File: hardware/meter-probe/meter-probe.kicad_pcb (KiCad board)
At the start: 4 copper layers, 40 x 68 mm, 52 parts, among them J1 Cable, SW1 Sensor Button, U1 TSL2585, U2 USBLC6-2SC6, U3 MIC5365-1.8YC5, U4 FT260Q, U5 CAT24C08

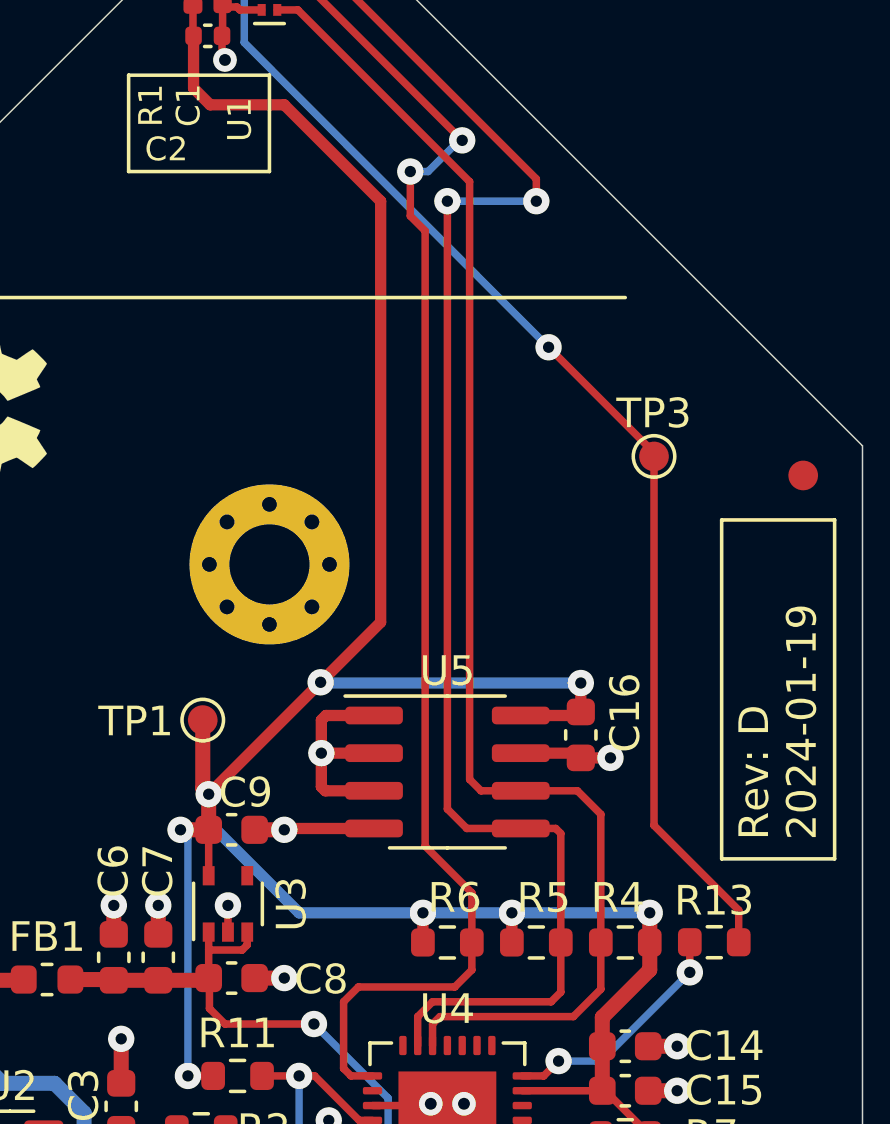
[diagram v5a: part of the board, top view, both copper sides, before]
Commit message: Change footprint of meter probe EEPROM
This change is for a smaller package, to better fit within enclosure
size constraints that limit height above the board on the front half.
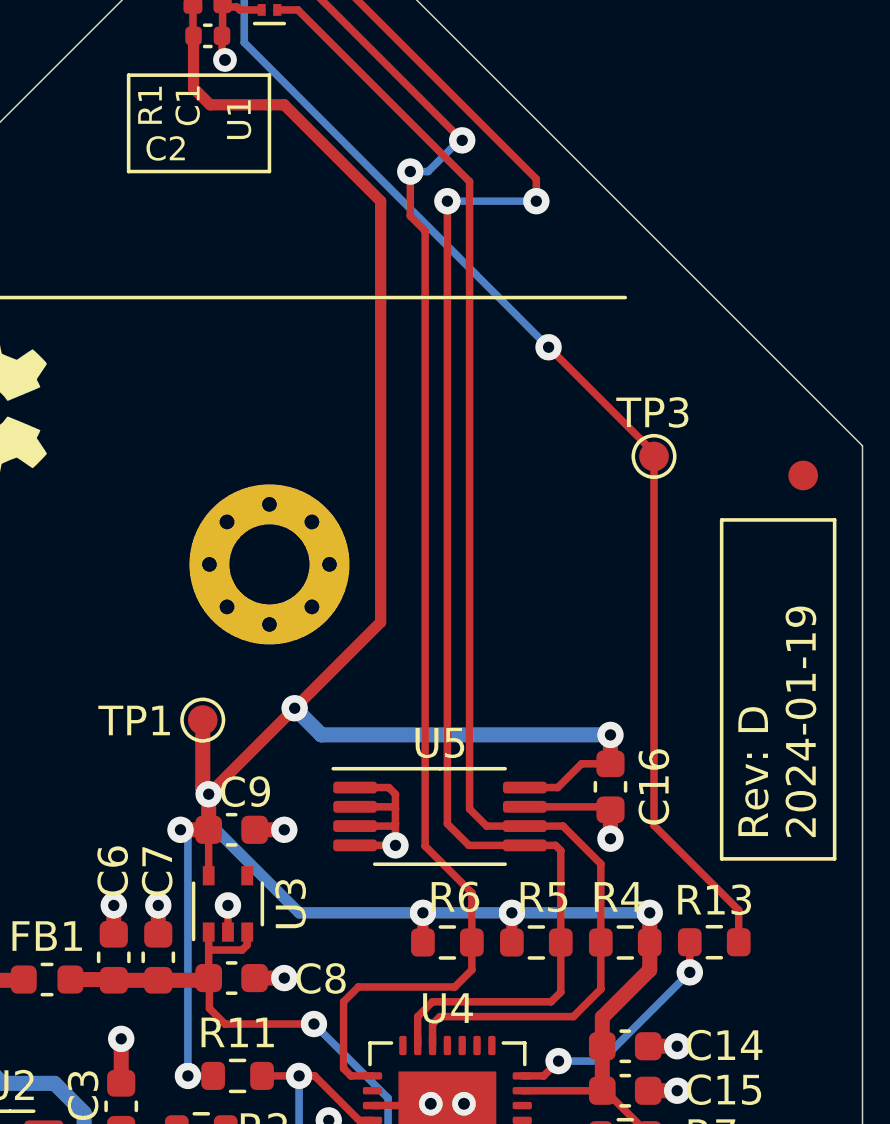
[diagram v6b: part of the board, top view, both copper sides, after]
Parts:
- U5: footprint Package_SO:SOIC-8_3.9x4.9mm_P1.27mm -> Package_SO:TSSOP-8_4.4x3mm_P0.65mm
- moved C16 2.02 mm to (131.5, 89.5)
- moved U5 1.52 mm to (125.8, 90.5)
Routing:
- net +1V8: track 93.8 -> 97.4 mm
- net GND: track 44.8 -> 42.3 mm

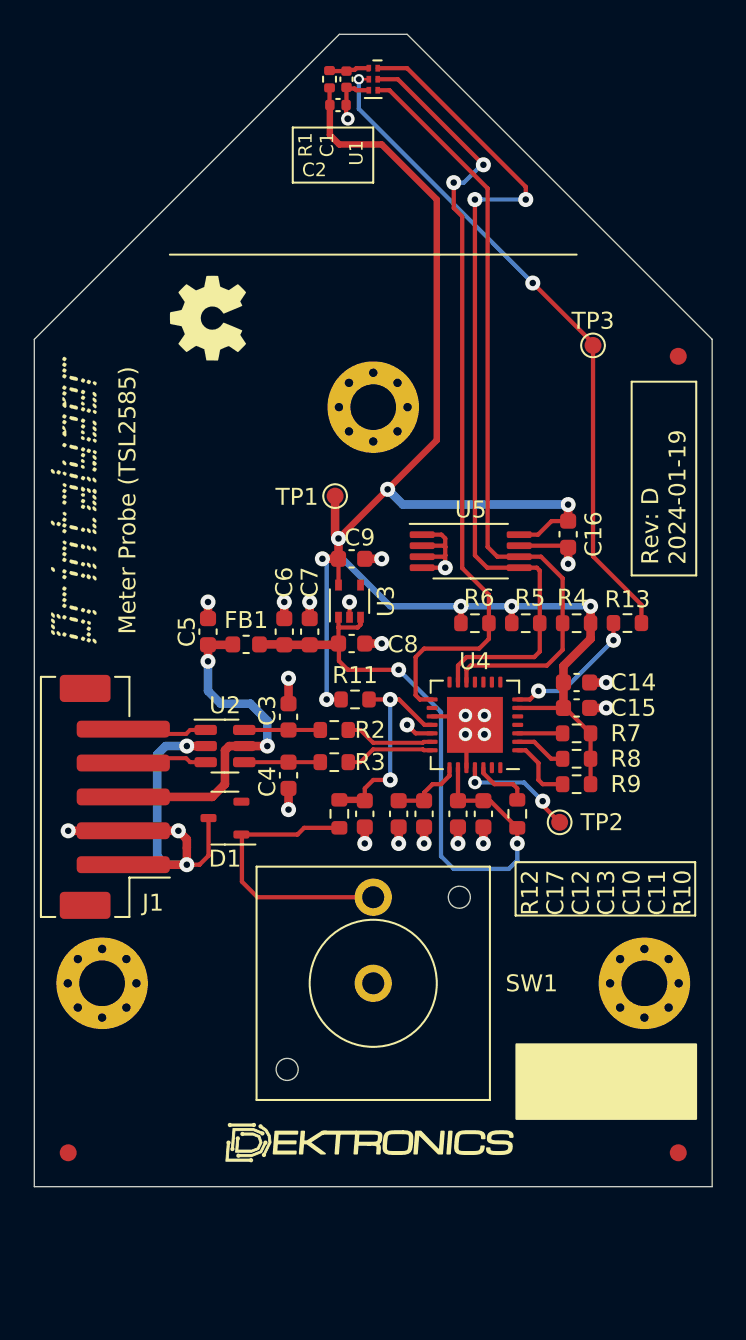
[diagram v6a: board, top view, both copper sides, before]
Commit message: Move meter probe cable connector downward a bit
This required a fair amount of rerouting around the TVS components.
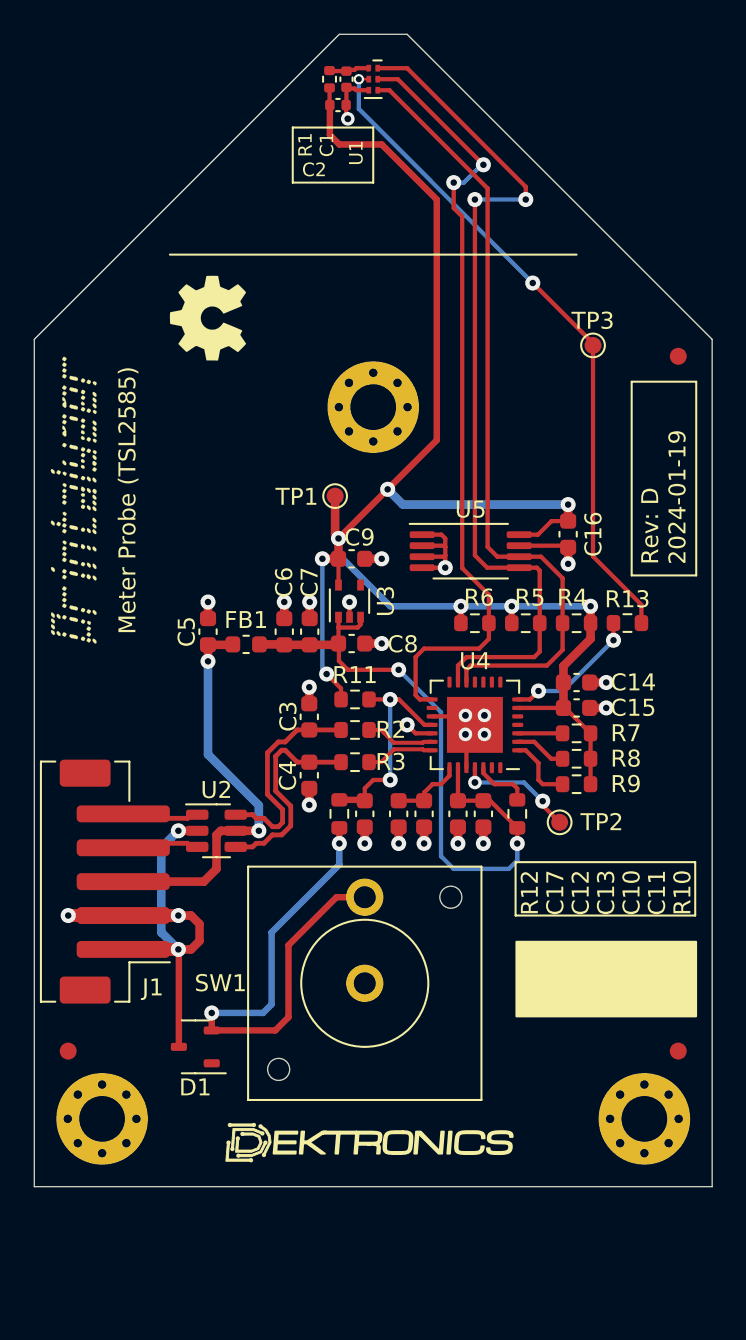
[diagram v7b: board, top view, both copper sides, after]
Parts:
- moved D1 13.6 mm to (109.5, 119.8)
- moved H1 8.00 mm to (104.0, 124.0)
- moved H2 8.00 mm to (136.0, 124.0)
- moved FID1 6.00 mm to (102.0, 120.0)
- moved FID2 6.00 mm to (138.0, 120.0)
- moved U2 5.02 mm to (110.8, 107.0)
- moved J1 5.00 mm to (104.8, 110.0)
- moved NT1 4.56 mm to (109.8, 113.0)
- moved C3 1.22 mm to (116.2, 100.3)
- moved C4 1.22 mm to (116.2, 103.7)
- moved R2 1.22 mm to (118.9, 101.0)
- moved R3 1.22 mm to (118.9, 103.0)
- moved SW1 0.50 mm to (119.5, 116.0)
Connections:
- D1 pad 1: Net-(D1-K-Pad1) -> unconnected-(D1-K-Pad1)
- D1 pad 2: unconnected-(D1-K-Pad2) -> Net-(D1-K-Pad2)
- R12 pad 1: Net-(D1-K-Pad1) -> Net-(D1-K-Pad2)
- SW1 pad 2: Net-(D1-K-Pad1) -> Net-(D1-K-Pad2)
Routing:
- net Net-(D1-K-Pad2): track 0.00 -> 31.6 mm, vias 0 -> 2
- net Net-(D1-K-Pad1): track 16.8 -> 0.00 mm
- net /USB_DI+: track 4.41 -> 12.5 mm
- net /USB_DI-: track 4.41 -> 12.5 mm
- net VBUS: track 20.6 -> 24.3 mm
- net /USB_D-: track 5.29 -> 4.06 mm
- net /USB_D+: track 5.29 -> 4.06 mm
- net /USB_CONN_D+: track 2.50 -> 1.57 mm
- net /USB_CONN_D-: track 2.50 -> 1.57 mm
- net Earth: track 18.6 -> 19.5 mm

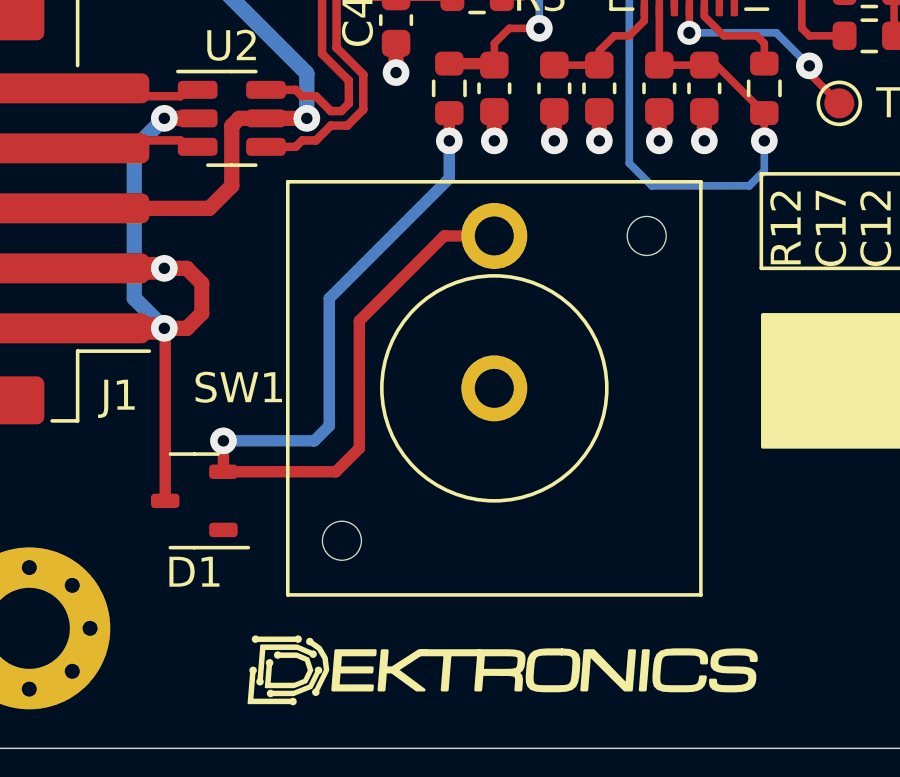
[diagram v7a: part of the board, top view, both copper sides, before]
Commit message: Fix meter probe button centering
Somehow the button managed to get 0.5mm off-center.
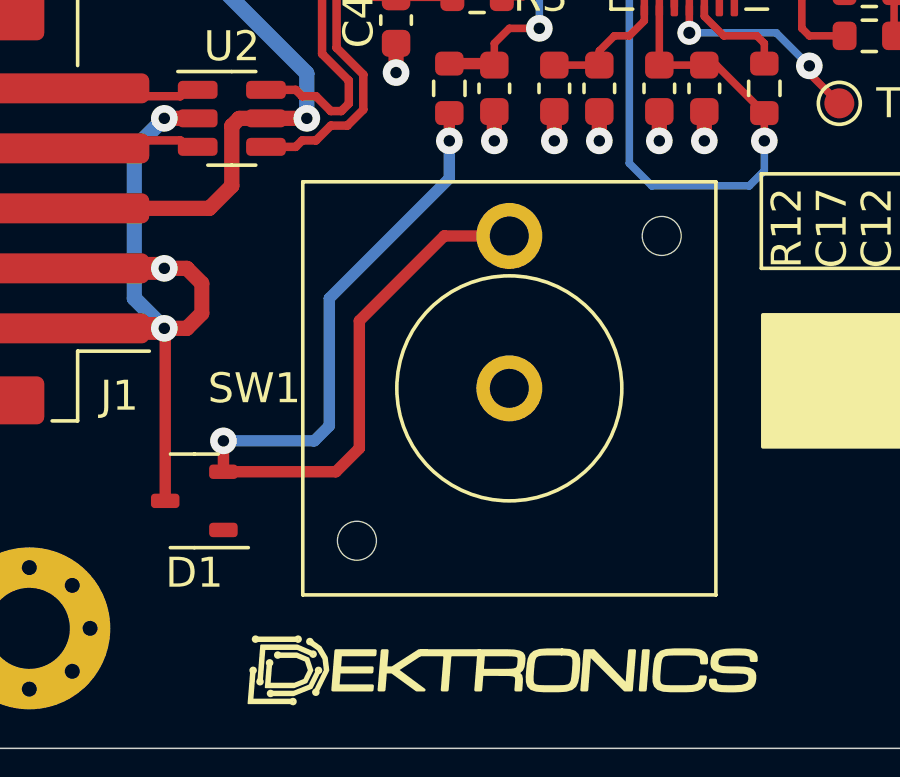
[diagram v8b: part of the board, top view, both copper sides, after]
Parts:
- moved SW1 0.50 mm to (120.0, 116.0)
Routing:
- net Net-(D1-K-Pad2): track 31.6 -> 32.1 mm
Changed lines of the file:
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@@
   )
   (footprint "lib_fp:SW_Key_6425_0101" locked (layer "F.Cu")
-    (at 119.5 116)
+    (at 120 116)
     (descr "SW PUSH SMALL http://www.ckswitches.com/media/1457/ksa_ksl.pdf")
     (tags "SW PUSH SMALL Tactile C&K")
@@
   (gr_circle (center 120 62) (end 120 58)
     (stroke (width 0.1) (type default)) (fill none) (layer "Cmts.User"))
-  (gr_line (start 140 88) (end 98.25 88)
+  (gr_line (start 140 88) (end 100 88)
     (stroke (width 0.1) (type default)) (layer "Cmts.User"))
   (gr_line (start 108 73) (end 132 73)
@@
   (segment (start 123 105.225) (end 121.5 105.225) (width 0.254) (layer "F.Cu") (net 7))
   (segment (start 123 104.75) (end 123.5 104.25) (width 0.254) (layer "F.Cu") (net 7))
+  (segment (start 117.83 110.92) (end 120 110.92) (width 0.381) (layer "F.Cu") (net 8))
   (segment (start 118 107.75) (end 118 106.825) (width 0.381) (layer "F.Cu") (net 8))
-  (segment (start 119.5 110.92) (end 117.83 110.92) (width 0.381) (layer "F.Cu") (net 8))
   (segment (start 110.47 117.75) (end 110.47 118.78) (width 0.381) (layer "F.Cu") (net 8))
   (segment (start 115 113.75) (end 115 118) (width 0.381) (layer "F.Cu") (net 8))
